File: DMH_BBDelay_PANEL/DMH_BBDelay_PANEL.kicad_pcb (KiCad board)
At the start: 2 copper layers, 100 x 200 mm, 34 parts, among them J0 Panel_GND_Solder_Wire_Pad

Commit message: FInalized panel design
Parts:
- H18: value Clock Sync A -> Clk Sync A
- H19: value Clock Sync B -> Clk Sync B
- H20: value Input A -> In A
- H21: value Input B -> In B
- H22: value Output A -> Out A
- H23: value Output B -> Out B
- H25: value FB CV B -> FB B CV
- H34: value Clock A -> Clk A
- H35: value Clock B -> Clk B
- H5: value Time A&B -> Time
- H7: value FB CV A -> FB A CV
- moved H22 85.0 mm to (58.5, 208.8)
- moved H21 84.5 mm to (141.0, 190.2)
- moved H32 50.0 mm to (75.0, 190.2)
- moved H31 33.0 mm to (124.5, 208.8)
- moved H35 33.0 mm to (108.0, 208.8)
- moved H14 28.0 mm to (62.8, 140.0)
- moved H15 28.0 mm to (137.2, 140.0)
- moved H25 28.0 mm to (112.5, 168.0)
- moved H7 28.0 mm to (87.5, 168.0)
- moved H30 24.8 mm to (75.0, 208.8)
- moved H34 24.8 mm to (91.5, 208.8)
- moved H10 24.8 mm to (87.5, 140.0)
- moved H11 24.8 mm to (112.5, 140.0)
- moved H16 24.8 mm to (137.2, 168.0)
- moved H17 24.8 mm to (62.8, 168.0)
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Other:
- board text added: "BBD"
- board text added: "Delay"
- board text removed: "Name"
- board text removed: "TYPE"

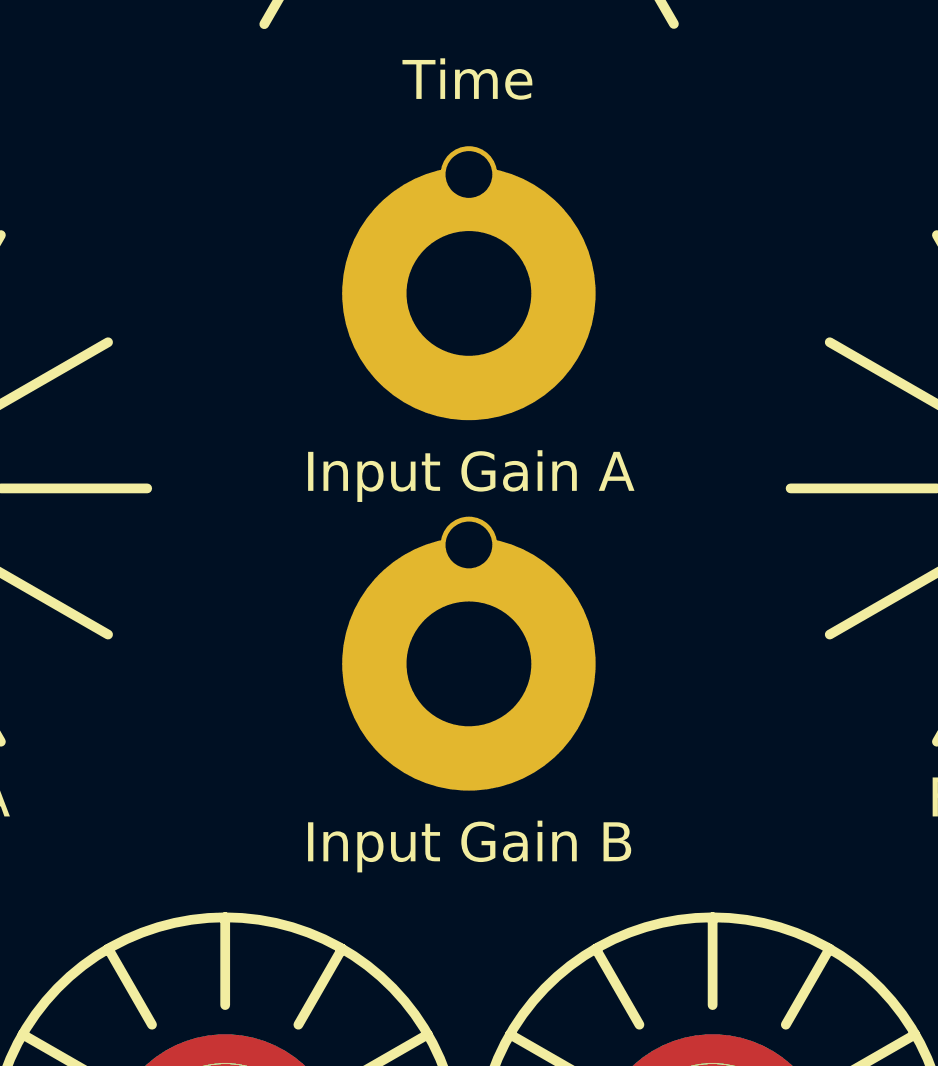
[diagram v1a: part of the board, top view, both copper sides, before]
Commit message: Added LEDs and Link switch
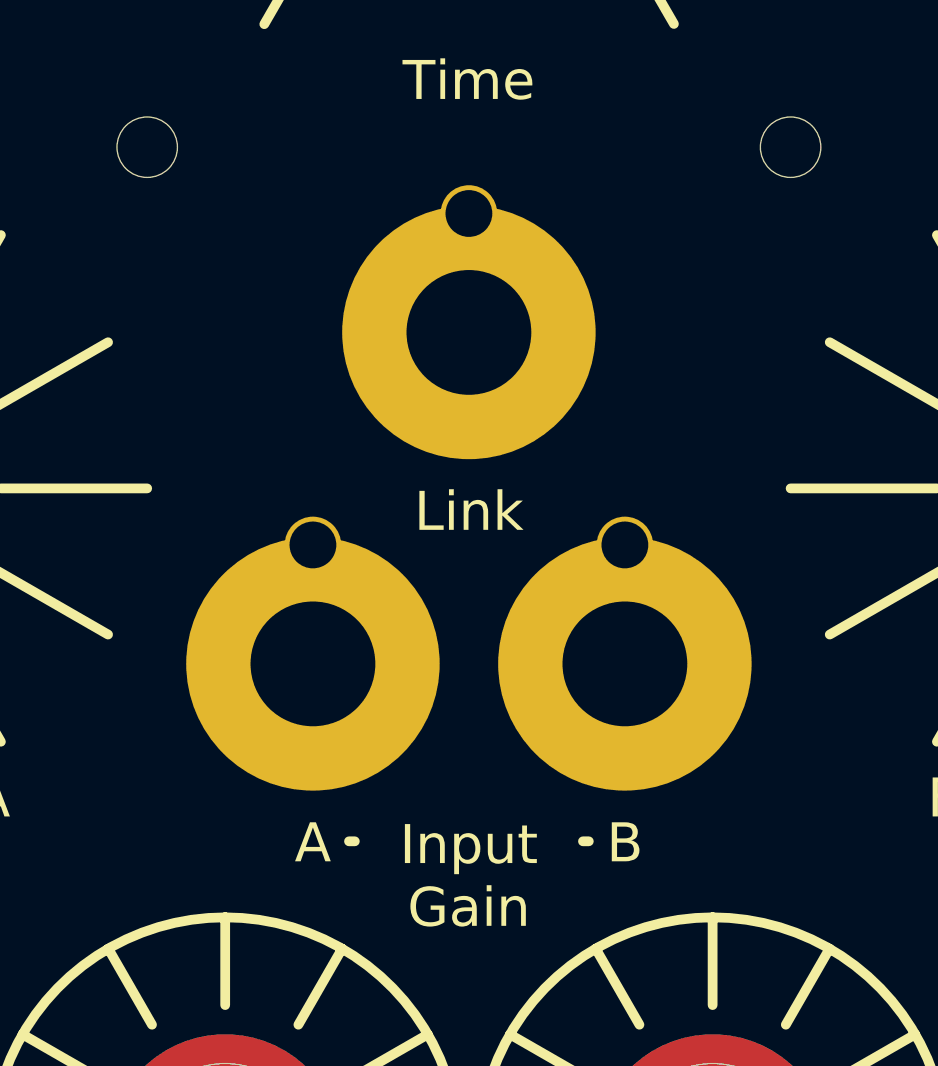
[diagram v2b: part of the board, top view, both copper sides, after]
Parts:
- added H28: LED_A, SynthStuff:MountingHole_LED_3mm_R, F.Cu at (83.5, 88.5)
- added H29: LED_B, SynthStuff:MountingHole_LED_3mm_R, F.Cu at (116.5, 88.5)
- added H36: Link, SynthStuff:Toggle_Switch_TE_Cutout, F.Cu at (100.0, 98.0)
- H12: value Input Gain A -> A
- H13: value Input Gain B -> B
- moved H12 20.6 mm to (92.0, 115.0)
- moved H13 8.00 mm to (108.0, 115.0)
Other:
- board text added: "Input Gain"

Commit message: Update DMH_BBDelay_PANEL.kicad_pcb
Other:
- board text added: "Up is ping-pong"
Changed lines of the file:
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@@
+		)
+	)
+	(gr_text "Up is ping-pong"
+		(at 100 89.1 0)
+		(layer "Cmts.User")
+		(effects
+			(font
+				(size 1 1)
+				(thickness 0.15)
+			)
 		)
 	)

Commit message: Added tone knob
... by making Input Gain switch to span both channels. Also added a center Linked LED
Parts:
- removed H13: B, SynthStuff:Toggle_Switch_TE_Cutout
- added H37: Tone, SynthStuff:Pot_Cutout_Tiny_text_P110KH1, F.Cu at (100.0, 114.0)
- added H38: LED_L, SynthStuff:MountingHole_LED_3mm_B, F.Cu at (100.0, 97.5)
- H12: value A -> Gain
- moved H12 23.6 mm to (90.0, 91.5)
- moved H36 11.9 mm to (110.0, 91.5)
- moved H28 5.15 mm to (81.0, 84.0)
- moved H29 5.15 mm to (119.0, 84.0)
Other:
- board text removed: "Input Gain"
